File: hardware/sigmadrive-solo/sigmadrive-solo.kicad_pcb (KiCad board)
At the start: 4 copper layers, 72 x 87.3 mm, 135 parts, among them J1 CONN_01X02, J10 Conn_01x03, J11 Conn_01x03, J12 Conn_01x05, J2 CONN_02X05, J3 CONN_01X03, J4 Conn_01x03, J5 Conn_01x05, J6 629_105_150_921, J7 CONN_01X02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

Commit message: Rerouted ADC and encoder connectors
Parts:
- removed C29: 4.7uF 25V, Capacitor_SMD:C_0805_2012Metric
- added D6: GREEN, LED_SMD:LED_0603_1608Metric, F.Cu at (100.8, 59.7)
- added R21: 2.2k, Resistor_SMD:R_0603_1608Metric, F.Cu at (100.8, 58.2)
- R6: moved to B.Cu
- moved R6 11.8 mm to (108.9, 44.3), turned to 270 degrees
- moved R2 6.28 mm to (108.0, 40.2)
- moved R88 5.70 mm to (125.4, 45.3), turned to 270 degrees
- moved J2 5.31 mm to (115.5, 35.6), turned to 270 degrees
- moved R5 4.61 mm to (112.9, 40.2)
- moved R3 4.51 mm to (111.4, 40.2)
- moved R40 3.80 mm to (126.9, 45.3)
- moved SW1 3.06 mm to (116.8, 49.6), turned to 270 degrees
- moved R11 2.92 mm to (110.5, 51.9)
- moved R12 2.92 mm to (112.0, 51.9)
- moved R38 2.50 mm to (123.9, 45.3)
- moved R44 2.15 mm to (114.5, 40.2)
- moved D5 1.49 mm to (109.9, 40.2), turned to 270 degrees
- moved C24 1.22 mm to (119.3, 66.0)
- moved R90 0.30 mm to (142.3, 47.6)
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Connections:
- R2 pad 1: /MCU/PB7 -> /MCU/PA10
- R3 pad 1: /MCU/PB6 -> /MCU/PA9
- SW1 pad 1: +3V3 -> /MCU/A_TERM_R120
- SW1 pad 3: /MCU/B_TERM_R120 -> +3V3
- SW1 pad 6: /MCU/A_TERM_R120 -> /MCU/GPIO_CONF_1
- SW1 pad 8: /MCU/GPIO_CONF_1 -> /MCU/B_TERM_R120
- U5 pad 18: /MCU/PC3 -> /MCU/VBAT_ADC
- U5 pad 23: /MCU/ENCODER_A -> /MOSFETs/DRV_SOC
- U5 pad 24: /MCU/ENCODER_B -> /MOSFETs/DRV_SOB
- U5 pad 25: /MCU/ENCODER_Z -> /MOSFETs/DRV_SOA
- U5 pad 26: /MCU/DRV2_CS -> /MCU/PA3
- U5 pad 29: /MCU/DRV1_CS -> /MCU/PA4
- U5 pad 30: /MOSFETs/DRV_SOC -> /MCU/PA5
- U5 pad 31: /MOSFETs/DRV_SOB -> /MCU/PA6
- U5 pad 32: /MOSFETs/DRV_SOA -> /MCU/PA7
- U5 pad 33: /MCU/DRV_FAULT -> /MCU/PC4
- U5 pad 34: /MCU/VBAT_ADC -> /MCU/PC5
- U5 pad 7: /MCU/PC13 -> /MCU/DRV1_CS
- U5 pad 8: /MCU/PC14 -> /MCU/DRV2_CS
- U5 pad 9: /MCU/PC15 -> /MCU/DRV_FAULT
- U5 pad 91: /MCU/PB5 -> /MCU/ENCODER_Z
- U5 pad 92: /MCU/PB6 -> /MCU/ENCODER_A
- U5 pad 93: /MCU/PB7 -> /MCU/ENCODER_B
- U5 pad 97: /MCU/GPIO_CONF_2 -> /MCU/GPIO_CONF_1
- U5 pad 98: /MCU/GPIO_CONF_1 -> /MCU/GPIO_CONF_2
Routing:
- net VIN: track 126.3 -> 144.5 mm
- net /MCU/ENCODER_A: track 50.4 -> 32.4 mm, vias 1 -> 0
- net /MCU/PA9: track 0.00 -> 16.0 mm, vias 0 -> 1
- net /MCU/DRV2_CS: track 28.2 -> 42.9 mm
- net /MCU/PA14: track 17.3 -> 30.9 mm, vias 0 -> 1
- net /MCU/DRV_FAULT: track 26.9 -> 39.6 mm
- net /MCU/PA10: track 0.00 -> 12.5 mm, vias 0 -> 1
- net /MCU/PA13: track 19.7 -> 29.7 mm, vias 2 -> 1
- net /MCU/ENCODER_Z: track 48.8 -> 39.7 mm
- net /MCU/DRV1_CS: track 25.3 -> 34.4 mm
- net +3V3: track 355.8 -> 347.9 mm, vias 19 -> 18
- net /MCU/PB7: track 7.72 -> 0.00 mm, vias 1 -> 0
- net Net-(J2-Pad6): track 11.1 -> 3.41 mm
- net /MCU/PB6: track 7.59 -> 0.00 mm, vias 1 -> 0
- net Net-(J2-Pad5): track 4.03 -> 10.6 mm
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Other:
- board text added: "BOOT_0"
- board text added: "CONF_1"
- board text added: "CONF_2"
- board text added: "PWR"
- board text added: "R120"
- board text added: "SIGMADRIVE-SOLO Ver 3.0"
- board text removed: "SIGMADRIVE-48V Ver 3.0"

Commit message: Added test points.
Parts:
- added D7: STPS0560Z, Diode_SMD:D_SOD-123, B.Cu at (93.8, 64.7)
- added TP1: PAD, TestPoint:TestPoint_Pad_D1.0mm, F.Cu at (95.6, 86.8)
- added TP2: PAD, TestPoint:TestPoint_Pad_D1.0mm, F.Cu at (97.9, 86.8)
- added TP3: PAD, TestPoint:TestPoint_Pad_D1.0mm, F.Cu at (95.3, 102.7)
- added TP4: PAD, TestPoint:TestPoint_Pad_D1.0mm, F.Cu at (115.2, 86.8)
- added TP5: PAD, TestPoint:TestPoint_Pad_D1.0mm, F.Cu at (103.7, 86.8)
- added TP6: PAD, TestPoint:TestPoint_Pad_D1.0mm, F.Cu at (110.4, 102.7)
- added TP7: PAD, TestPoint:TestPoint_Pad_D1.0mm, F.Cu at (119.9, 86.8)
- added TP8: PAD, TestPoint:TestPoint_Pad_D1.0mm, F.Cu at (123.1, 86.8)
- added TP9: PAD, TestPoint:TestPoint_Pad_D1.0mm, F.Cu at (121.4, 102.7)
- D5: value BAT30KFILM -> STPS0560Z; footprint Diode_SMD:D_SOD-523 -> Diode_SMD:D_SOD-123; moved to B.Cu
- moved D5 27.4 mm to (93.8, 62.3), turned to 180 degrees
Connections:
- C26 pad 1: +5V -> Net-(C26-Pad1)
- L2 pad 2: +5V -> Net-(C26-Pad1)
- R18 pad 2: +5V -> Net-(C26-Pad1)
- U5 pad 23: /MOSFETs/DRV_SOC -> /MOSFETs/DRV_SOA
- U5 pad 25: /MOSFETs/DRV_SOA -> /MOSFETs/DRV_SOC
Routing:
- net /MCU/EXT_5V: track 9.72 -> 53.5 mm, vias 0 -> 2
- net +5V: track 209.6 -> 194.0 mm, vias 5 -> 3
- net Net-(C26-Pad1): track 0.00 -> 13.6 mm, vias 0 -> 2
- net +3V3: track 347.9 -> 339.2 mm
- net GND: track 99.5 -> 94.5 mm
- net /MCU/PB4: track 17.4 -> 14.0 mm
- net /MOSFETs/DRV_SOA: track 33.4 -> 35.9 mm
- net /MCU/DRV2_CS: track 42.9 -> 45.2 mm
- net Net-(R12-Pad2): track 45.4 -> 47.4 mm
- net /MCU/PB13: track 29.3 -> 30.1 mm
- net /MOSFETs/DRV_SOC: track 39.0 -> 38.3 mm
- net /MCU/ENCODER_RO: track 29.0 -> 29.5 mm
- net PGND: vias 47 -> 49
- added copper zone on F.Cu, net Net-(C26-Pad1)
- removed copper zone on F.Cu, net +5V

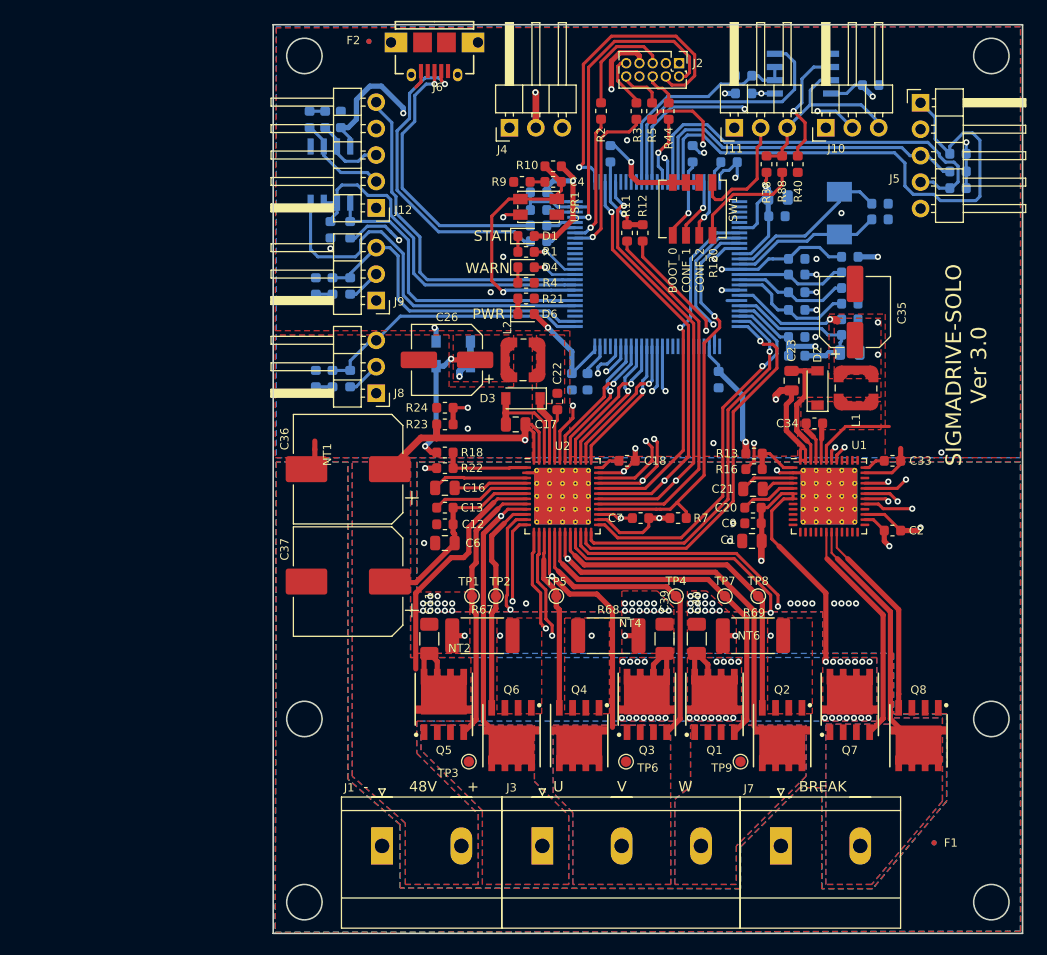
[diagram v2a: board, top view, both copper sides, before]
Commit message: Adding capacitors on the current sense lines.
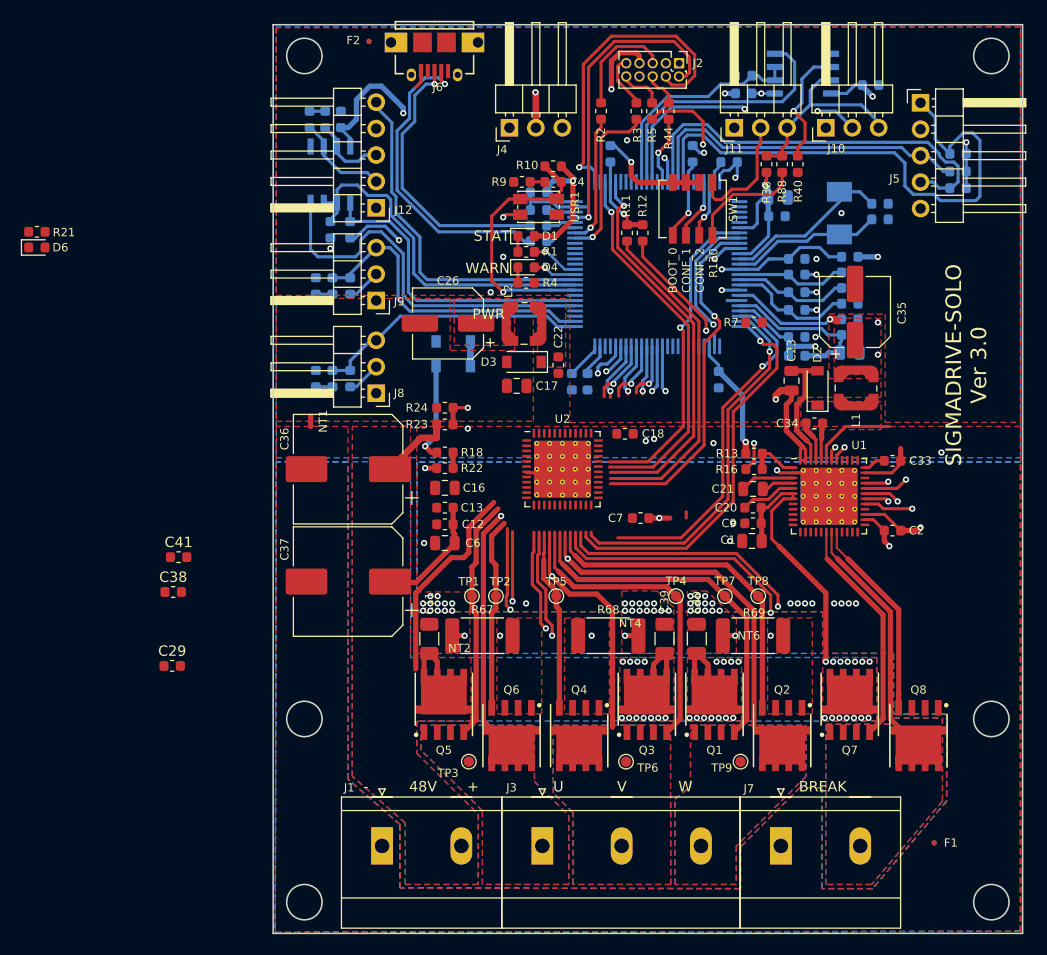
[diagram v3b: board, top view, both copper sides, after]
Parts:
- added C29: 100pF, Capacitor_SMD:C_0603_1608Metric, F.Cu at (66.8, 93.5)
- added C38: 100pF, Capacitor_SMD:C_0603_1608Metric, F.Cu at (66.9, 86.4)
- added C41: 100pF, Capacitor_SMD:C_0603_1608Metric, F.Cu at (67.4, 83.1)
- C12, C2, C22, C34, C7, C9: value 100nF -> 100nF 50V
- Q1, Q2, Q3, Q4, Q5, Q6, Q7, Q8: value STL160NS3LLH7 -> NTMFS5C628NLT1G
- R46, R49, R52: value 4.7k -> 3.3k
- moved D6 47.4 mm to (53.8, 53.3)
- moved R21 47.4 mm to (53.8, 51.8)
- moved R7 20.2 mm to (122.7, 60.5), turned to 180 degrees
- moved C17 3.70 mm to (99.9, 66.6)
- moved C22 3.50 mm to (103.9, 64.6)
- moved D3 3.50 mm to (100.6, 64.3)
- moved C26 3.50 mm to (93.3, 60.6)
- moved L2 3.50 mm to (100.6, 60.6)
- moved NT1 3.22 mm to (80.1, 70.0)
- moved C18 2.61 mm to (110.3, 71.2)
- moved U2 2.60 mm to (104.3, 74.6)
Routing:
- net VIN: track 144.4 -> 79.7 mm, vias 38 -> 36
- net +3V3: track 339.2 -> 304.6 mm, vias 18 -> 17
- net GND: track 94.5 -> 64.5 mm, vias 20 -> 16
- net +5V: track 194.0 -> 183.8 mm, vias 3 -> 2
- net Net-(C13-Pad2): track 9.40 -> 0.00 mm
- net Net-(C16-Pad2): track 9.22 -> 0.00 mm
- net /MCU/GATE_ENABLE: track 55.9 -> 46.9 mm, vias 4 -> 3
- net /MCU/PWM_AL: track 14.0 -> 5.59 mm
- net /MCU/PWM_AH: track 13.2 -> 4.77 mm
- net /MCU/PWM_BH: track 13.4 -> 5.18 mm
- net /MCU/DRV_CAL: track 20.5 -> 12.5 mm
- net /MCU/PWM_BL: track 14.0 -> 6.18 mm
- net /MCU/PWM_CL: track 13.9 -> 6.22 mm
- net /MCU/PWM_CH: track 13.4 -> 5.77 mm
- net Net-(C16-Pad1): track 7.10 -> 0.00 mm
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
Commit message: Work on sigmadrive-solo 3.1
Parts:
- added C42: 100pF, Capacitor_SMD:C_0603_1608Metric, B.Cu at (120.2, 68.1)
- added C43: 100pF, Capacitor_SMD:C_0603_1608Metric, B.Cu at (123.2, 68.1)
- added C44: 100pF, Capacitor_SMD:C_0603_1608Metric, B.Cu at (126.2, 68.1)
- added R25: 0, Resistor_SMD:R_0603_1608Metric, B.Cu at (82.4, 52.9)
- added R26: 28k, Resistor_SMD:R_0603_1608Metric, F.Cu at (92.5, 70.6)
- added R27: 21, Resistor_SMD:R_0603_1608Metric, B.Cu at (124.7, 68.1)
- added R29: 21, Resistor_SMD:R_0603_1608Metric, B.Cu at (121.7, 68.1)
- added R31: 21, Resistor_SMD:R_0603_1608Metric, B.Cu at (118.7, 68.1)
- added U4: TPD4S009, Package_SO:TSSOP-10_3x3mm_P0.5mm, F.Cu at (116.9, 75.9)
- R40: moved to B.Cu
- moved R21 89.4 mm to (142.1, 66.1), turned to 0 degrees
- moved D6 89.0 mm to (142.1, 64.6), turned to 180 degrees
- moved C29 42.0 mm to (106.8, 80.8), turned to 315 degrees
- moved C38 34.6 mm to (101.0, 80.8), turned to 225 degrees
- moved C41 31.4 mm to (98.7, 80.8), turned to 45 degrees
- moved R23 27.1 mm to (117.8, 81.3), turned to 180 degrees
- moved R24 25.1 mm to (114.7, 81.3)
- moved R7 20.3 mm to (111.6, 77.5), turned to 90 degrees
- moved R40 11.6 mm to (133.9, 36.1), turned to 180 degrees
- moved J5 8.10 mm to (138.7, 47.5)
- moved R90 8.10 mm to (142.3, 55.7)
- moved R91 8.10 mm to (142.3, 54.1)
- moved R92 8.10 mm to (142.3, 52.4)
- moved C36 5.60 mm to (83.5, 80.2)
- moved C37 5.60 mm to (83.5, 91.0)
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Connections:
- C4 pad 2: /MCU/PD11 -> /MCU/PA8
- R10 pad 2: /MCU/PD11 -> /MCU/PA8
- U1 pad 33: /MCU/GATE_ENABLE -> /MCU/GATE2_ENABLE
- U2 pad 48: VIN -> Net-(R26-Pad2)
- U3 pad 2: /MCU/ENCODER_DE -> /MCU/ENCODER_RE
- U5 pad 23: /MOSFETs/DRV_SOA -> /MCU/PA0
- U5 pad 24: /MOSFETs/DRV_SOB -> /MCU/PA1
- U5 pad 25: /MOSFETs/DRV_SOC -> /MCU/PA2
- U5 pad 36: /MCU/PB1 -> /MCU/GATE2_ENABLE
- U5 pad 58: /MCU/PD11 -> /MCU/ENCODER_RE
- USR1 pad 2: /MCU/PD11 -> /MCU/PA8
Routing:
- net VIN: track 79.7 -> 134.5 mm, vias 36 -> 37
- net +3V3: track 304.6 -> 343.7 mm, vias 17 -> 19
- net GND: track 64.5 -> 97.9 mm, vias 16 -> 21
- net /MCU/ENCODER_RE: track 0.00 -> 32.2 mm
- net /MCU/GATE_ENABLE: track 46.9 -> 16.7 mm, vias 3 -> 2
- net /MCU/GATE2_ENABLE: track 0.00 -> 30.0 mm, vias 0 -> 2
- net /MCU/PD11: track 25.7 -> 0.00 mm, vias 1 -> 0
- net /MCU/ENCODER_B: track 52.7 -> 35.4 mm, vias 0 -> 1
- net /MCU/PA8: track 0.00 -> 15.5 mm, vias 0 -> 1
- net /MOSFETs/DRV_SOC: track 38.0 -> 23.7 mm
- net /MCU/PA2: track 0.00 -> 12.0 mm
- net /MOSFETs/DRV_SOB: track 36.0 -> 24.4 mm
- net /MCU/PA0: track 0.00 -> 11.0 mm
- net /MCU/PA1: track 0.00 -> 10.6 mm
- net Net-(C13-Pad2): track 0.00 -> 10.4 mm
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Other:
- outline, holes or cut-outs redrawn
- board text added: "SIGMADRIVE-SOLO Ver 3.1"
- board text removed: "SIGMADRIVE-SOLO Ver 3.0"

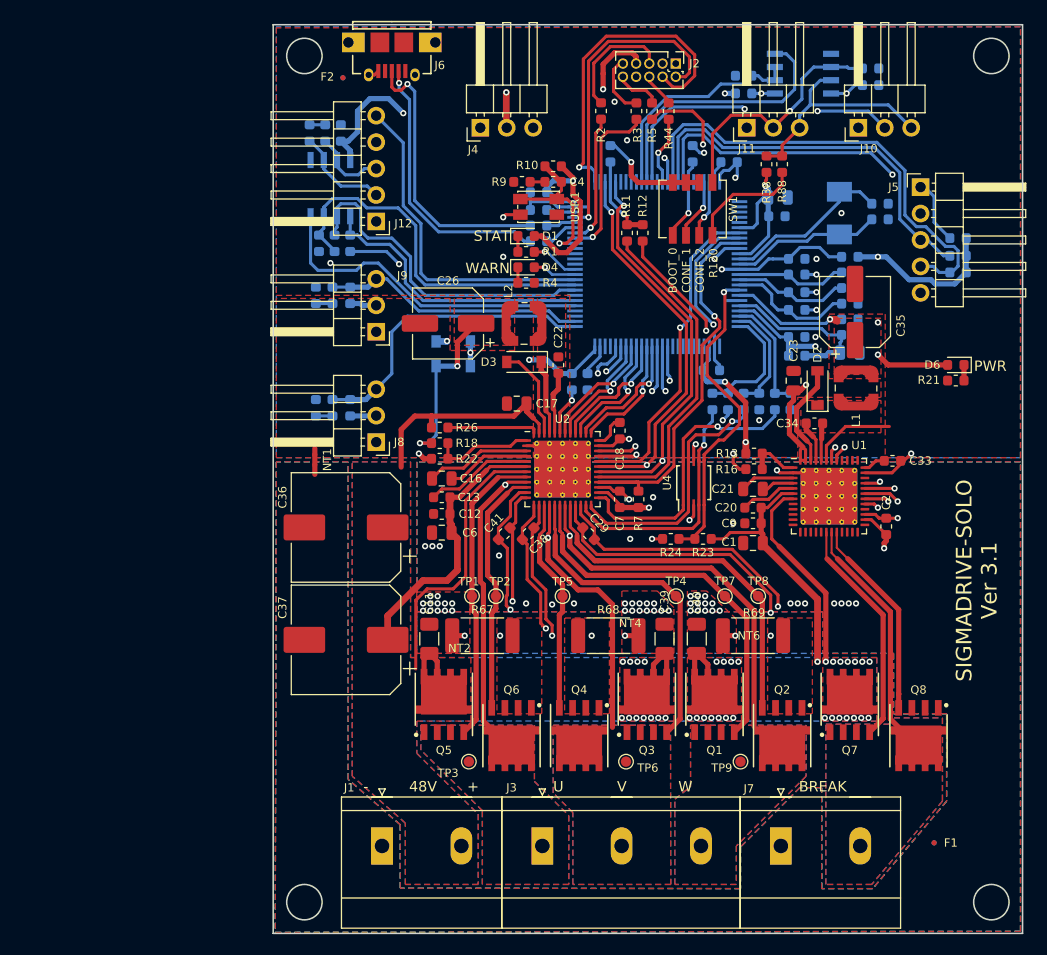
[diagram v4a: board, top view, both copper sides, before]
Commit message: Updated Inductor footprints. Split RE/DE for RS485.
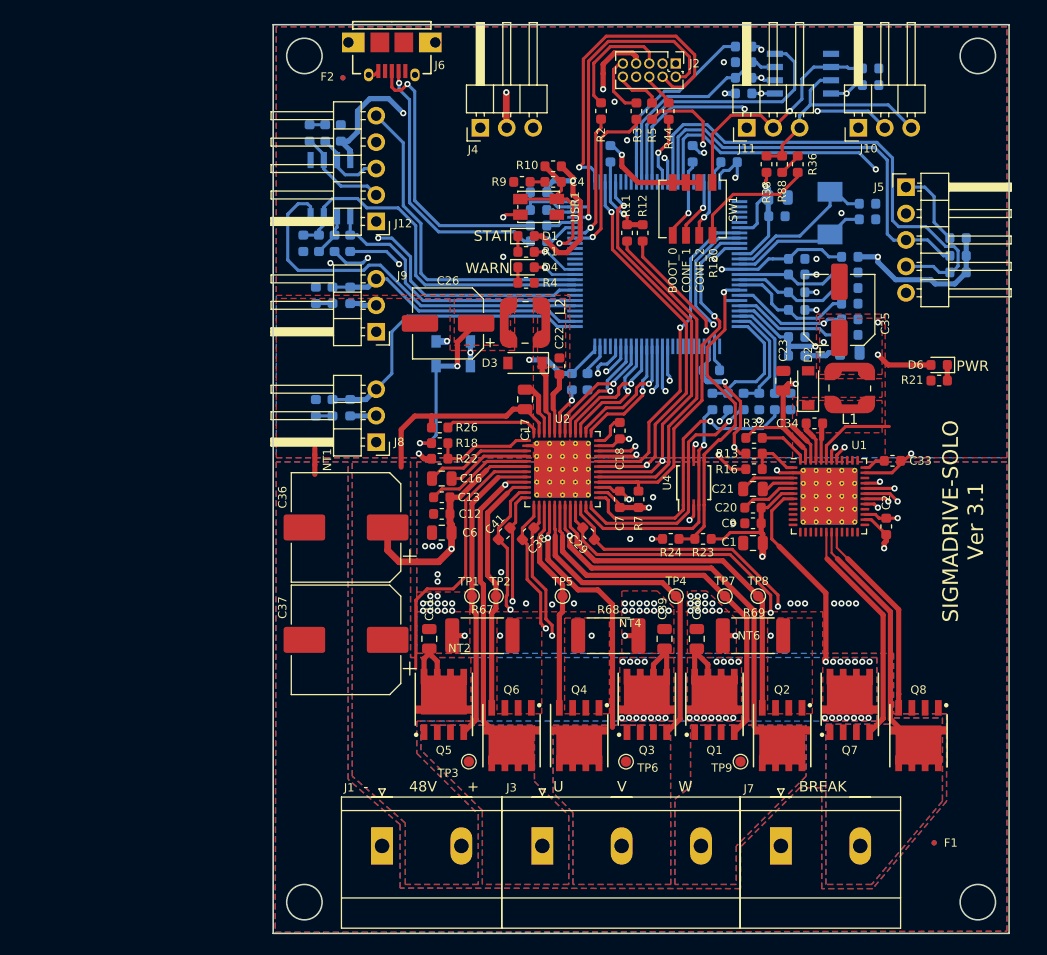
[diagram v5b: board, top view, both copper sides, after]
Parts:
- added R32: 28k, Resistor_SMD:R_0603_1608Metric, F.Cu at (122.7, 71.6)
- added R33: 0, Resistor_SMD:R_0603_1608Metric, B.Cu at (82.4, 52.9)
- added R34: 0, Resistor_SMD:R_0603_1608Metric, B.Cu at (121.7, 34.0)
- added R35: 0, Resistor_SMD:R_0603_1608Metric, B.Cu at (121.7, 37.0)
- added R36: 21, Resistor_SMD:R_0603_1608Metric, F.Cu at (126.9, 45.3)
- C11, C39, C40: footprint Capacitor_SMD:C_1206_3216Metric -> Capacitor_SMD:C_0805_2012Metric
- C29, C38, C41, C42, C43, C44: value 100pF -> 1000pF/50V
- FB1: value BEAD/0.6OHM/0.2A/2.2 kOhm @ 100MHz -> 0.6OHM/0.2A/2.2 kOhm @ 100MHz
- L1, L2: footprint Inductor_SMD:L_Wuerth_WE-TPC-3816 -> Sigmadrone:L_Wuerth_WE-TPC-4828
- moved D6 1.60 mm to (140.5, 64.6)
- moved R21 1.60 mm to (140.5, 66.1)
- moved C35 1.51 mm to (130.9, 59.3)
- moved R15 1.50 mm to (79.4, 52.9)
- moved R25 1.50 mm to (80.9, 52.9), turned to 270 degrees
- moved J5 1.40 mm to (137.3, 47.5)
- moved R85 1.30 mm to (121.7, 35.5)
- moved C27 1.20 mm to (133.6, 49.1)
- moved C32 1.20 mm to (133.6, 50.6)
- moved C23 1.00 mm to (125.5, 66.1)
- moved D2 0.90 mm to (127.9, 66.8)
- moved Y1 0.90 mm to (130.0, 50.0)
- moved C17 0.89 mm to (100.7, 67.9), turned to 90 degrees
- moved L1 0.60 mm to (131.9, 66.8)
- moved D3 0.14 mm to (100.7, 64.4)
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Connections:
- C29 pad 1: /MOSFETs/C_ISENSE_P -> /MOSFETs/C_ISENSE_N
- C29 pad 2: /MOSFETs/C_ISENSE_N -> /MOSFETs/C_ISENSE_P
- C38 pad 1: /MOSFETs/B_ISENSE_P -> /MOSFETs/B_ISENSE_N
- C38 pad 2: /MOSFETs/B_ISENSE_N -> /MOSFETs/B_ISENSE_P
- C41 pad 1: /MOSFETs/A_ISENSE_P -> /MOSFETs/A_ISENSE_N
- C41 pad 2: /MOSFETs/A_ISENSE_N -> /MOSFETs/A_ISENSE_P
- FB1 pad 1: +3V3 -> Net-(C30-Pad1)
- FB1 pad 2: Net-(C30-Pad1) -> +3V3
- R25 pad 2: /MCU/ENCODER_RE -> Net-(R25-Pad2)
- R88 pad 2: /MCU/B_TERM_R120 -> Net-(R36-Pad1)
- U1 pad 48: +5V -> Net-(R32-Pad2)
- U12 pad 2: /MCU/PD4 -> Net-(R34-Pad1)
- U3 pad 2: /MCU/ENCODER_RE -> Net-(R25-Pad2)
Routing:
- net /MCU/PD3: track 0.00 -> 18.4 mm
- net VIN: track 134.5 -> 147.8 mm, vias 37 -> 38
- net GND: track 97.9 -> 89.5 mm, vias 21 -> 22
- net Net-(R34-Pad1): track 0.00 -> 6.05 mm, vias 0 -> 2
- net /MCU/ENCODER_DI: track 32.2 -> 37.9 mm
- net +5V: track 192.0 -> 196.9 mm
- net Net-(R32-Pad2): track 0.00 -> 4.85 mm
- net Net-(R25-Pad2): track 0.00 -> 4.11 mm
- net +3V3: track 343.7 -> 340.0 mm
- net /MCU/ENCODER_RE: track 32.2 -> 28.9 mm, vias 0 -> 2
- net /MCU/ENCODER_Z: track 45.4 -> 47.8 mm
- net Net-(R36-Pad1): track 0.00 -> 2.20 mm
- net /MCU/ENCODER_A: track 38.3 -> 39.9 mm
- net Net-(C32-Pad1): track 14.5 -> 13.3 mm
- net /MCU/PD4: track 22.1 -> 21.1 mm
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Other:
- board size 72 x 87.3 mm -> 70.7 x 87.3 mm
